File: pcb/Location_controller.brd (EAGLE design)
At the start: 75 x 48 mm, 55 parts, among them IC1 LIS302DL

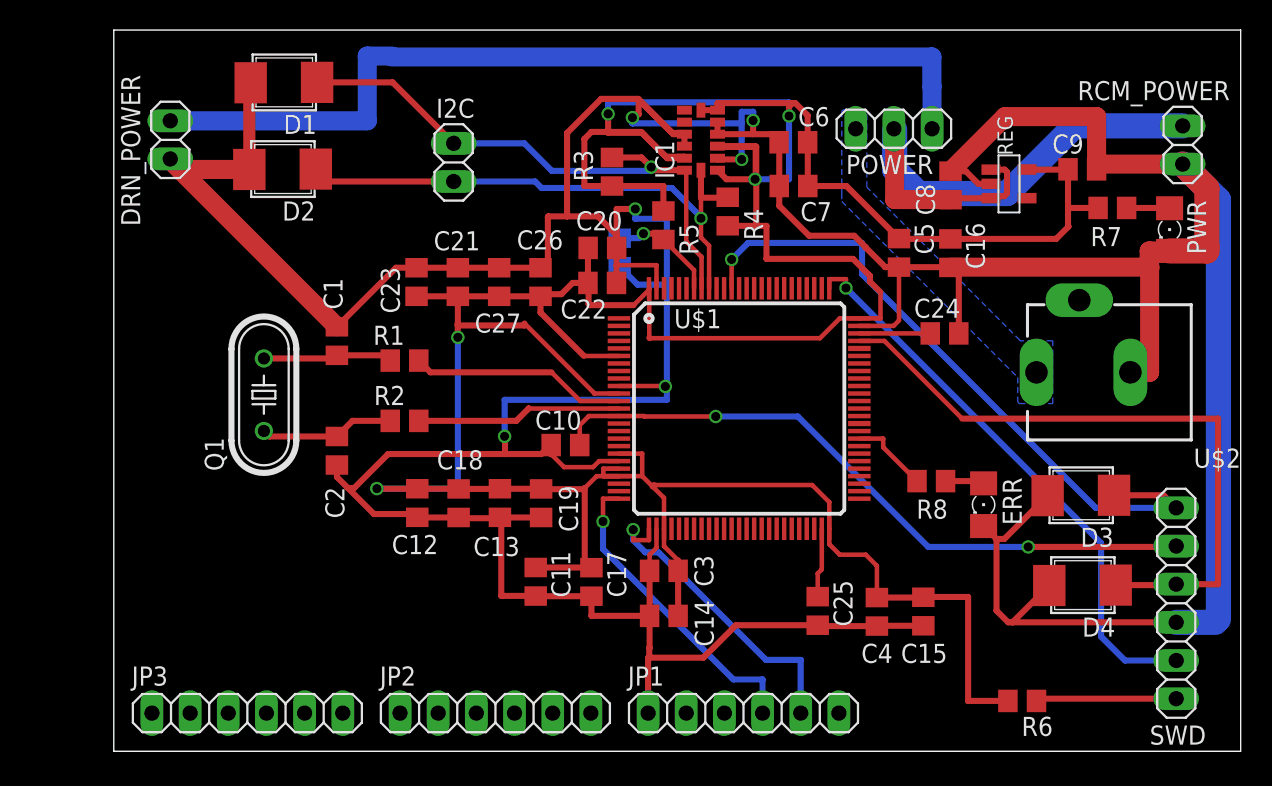
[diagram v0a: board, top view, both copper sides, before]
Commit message: Add TVS for I2C and USART connections
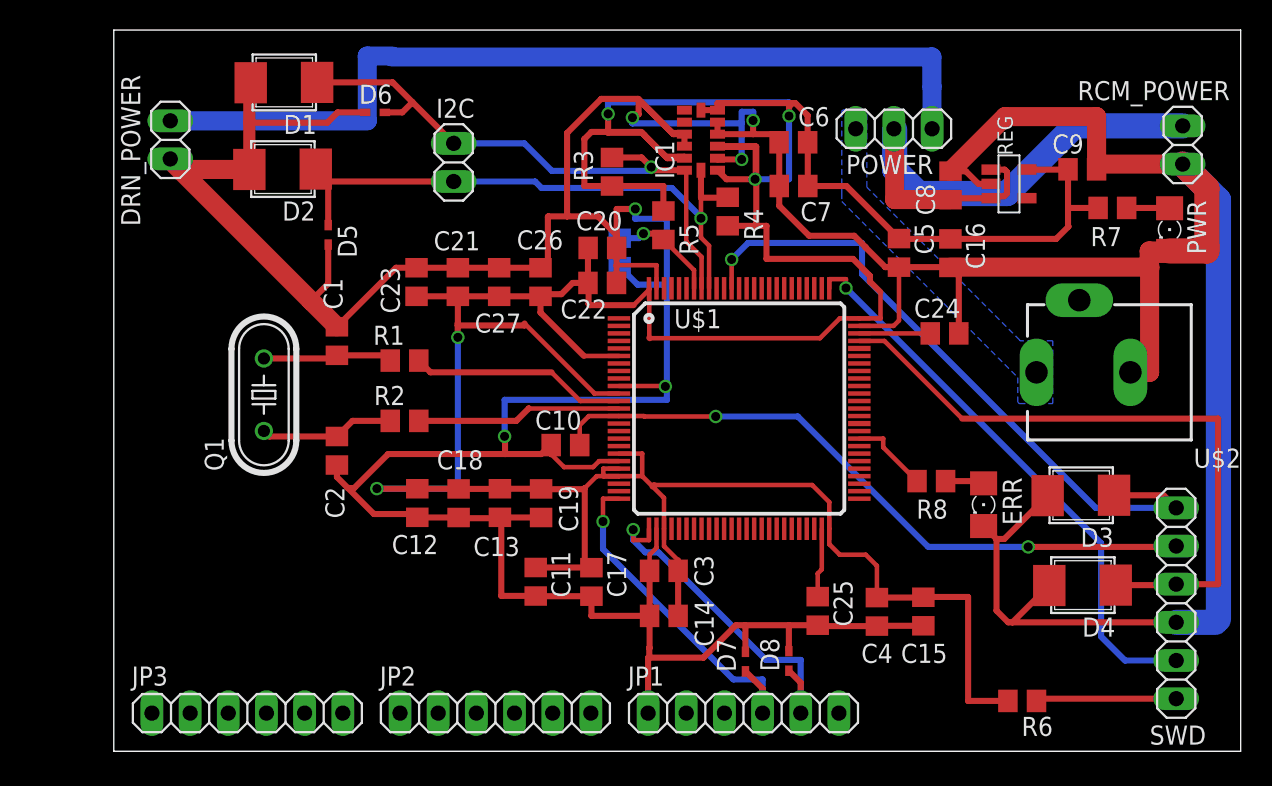
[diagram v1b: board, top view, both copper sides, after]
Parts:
- added D5, D6, D7, D8: (no value), diode:SOD523
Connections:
- net GND: now also D5.A, D6.A, D7.A, D8.A
- net I2C_SCL: now also D5.C
- net I2C_SDA: now also D6.C
- net USART2_RX: now also D8.C
- net USART2_TX: now also D7.C
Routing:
- net GND: track 371.4 -> 387.2 mm
- net USART2_TX: track 20.9 -> 24.1 mm
- net USART2_RX: track 21.2 -> 24.3 mm
- net I2C_SCL: track 36.9 -> 39.8 mm
- net I2C_SDA: track 38.6 -> 40.7 mm
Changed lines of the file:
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@@
 <element name="D4" library="stm32f4" package="SMB" value="ZDIODE" x="64.37" y="10.93" rot="R180"/>
 <element name="D3" library="stm32f4" package="SMB" value="ZDIODE" x="64.26" y="16.91" rot="R180"/>
+<element name="D5" library="diode" package="SOD523" value="" x="14.27" y="34.42" rot="R270"/>
+<element name="D6" library="diode" package="SOD523" value="" x="17.44" y="42.52" smashed="yes" rot="R180">
+<attribute name="NAME" x="18.535" y="44.365" size="1.27" layer="25" rot="R180"/>
+<attribute name="VALUE" x="18.075" y="44.425" size="1.27" layer="27" rot="R180"/>
+</element>
+<element name="D7" library="diode" package="SOD523" value="" x="42.04" y="5.92" rot="R90"/>
+<element name="D8" library="diode" package="SOD523" value="" x="44.93" y="5.96" rot="R90"/>
 </elements>
 <signals>
@@
 <wire x1="36.12" y1="13.54" x2="36.12" y2="14.81" width="0.3048" layer="1"/>
 <wire x1="35.66" y1="9.01" x2="35.66" y2="6.88" width="0.4064" layer="1"/>
-<wire x1="46.85" y1="8.39" x2="41.41" y2="8.39" width="0.4064" layer="1"/>
+<wire x1="46.85" y1="8.39" x2="44.93" y2="8.39" width="0.4064" layer="1"/>
+<wire x1="44.93" y1="8.39" x2="42.02" y2="8.39" width="0.4064" layer="1"/>
+<wire x1="42.02" y1="8.39" x2="41.41" y2="8.39" width="0.4064" layer="1"/>
 <wire x1="49.62" y1="28.31" x2="51.9" y2="28.31" width="0.3048" layer="1"/>
 <wire x1="51.9" y1="28.31" x2="52.26" y2="28.67" width="0.3048" layer="1"/>
@@
 <wire x1="65.21" y1="38.93" x2="65.41" y2="38.73" width="0.4064" layer="1"/>
 <wire x1="3.76" y1="39.42" x2="3.76" y2="39.34" width="0.4064" layer="1"/>
-<wire x1="3.76" y1="39.34" x2="14.85" y2="28.25" width="1.27" layer="1"/>
+<wire x1="3.76" y1="39.34" x2="13.125" y2="29.975" width="1.27" layer="1"/>
+<wire x1="13.125" y1="29.975" x2="14.85" y2="28.25" width="1.27" layer="1"/>
 <wire x1="70.71" y1="8.58" x2="73.32" y2="8.58" width="1.6764" layer="16"/>
 <wire x1="73.32" y1="8.58" x2="73.52" y2="8.78" width="0.4064" layer="16"/>
@@
 <contactref element="D2" pad="2"/>
 <wire x1="9.1118" y1="44.4916" x2="9.0218" y2="44.4916" width="0.4064" layer="1"/>
-<wire x1="9.0218" y1="44.4916" x2="9.0218" y2="38.7216" width="0.8128" layer="1"/>
+<wire x1="9.0218" y1="44.4916" x2="9.0218" y2="41.84" width="0.8128" layer="1"/>
+<wire x1="9.0218" y1="41.84" x2="9.0218" y2="38.7216" width="0.8128" layer="1"/>
 <wire x1="9.0218" y1="38.7216" x2="4.4584" y2="38.7216" width="1.27" layer="1"/>
 <wire x1="4.4584" y1="38.7216" x2="3.76" y2="39.42" width="0.4064" layer="1"/>
@@
 <wire x1="68.91" y1="32.22" x2="68.94" y2="32.22" width="1.27" layer="1"/>
 <wire x1="68.94" y1="32.22" x2="68.94" y2="25.22" width="1.27" layer="1"/>
+<contactref element="D6" pad="A"/>
+<contactref element="D5" pad="A"/>
+<wire x1="16.74" y1="42.52" x2="14.9" y2="42.52" width="0.4064" layer="1"/>
+<wire x1="14.9" y1="42.52" x2="14.22" y2="41.84" width="0.4064" layer="1"/>
+<wire x1="14.22" y1="41.84" x2="9.0218" y2="41.84" width="0.4064" layer="1"/>
+<wire x1="14.27" y1="33.72" x2="14.27" y2="31.12" width="0.4064" layer="1"/>
+<wire x1="14.27" y1="31.12" x2="13.125" y2="29.975" width="0.4064" layer="1"/>
+<contactref element="D7" pad="A"/>
+<contactref element="D8" pad="A"/>
+<wire x1="42.04" y1="6.62" x2="42.04" y2="8.37" width="0.4064" layer="1"/>
+<wire x1="42.04" y1="8.37" x2="42.02" y2="8.39" width="0.4064" layer="1"/>
+<wire x1="44.93" y1="6.66" x2="44.93" y2="8.39" width="0.4064" layer="1"/>
 </signal>
 <signal name="N$1">
@@
 <wire x1="13.4414" y1="38.747" x2="14.2684" y2="37.92" width="0.4064" layer="1"/>
 <wire x1="14.2684" y1="37.92" x2="22.62" y2="37.92" width="0.4064" layer="1"/>
+<contactref element="D5" pad="C"/>
+<wire x1="14.27" y1="35.02" x2="14.27" y2="37.9184" width="0.4064" layer="1"/>
+<wire x1="14.27" y1="37.9184" x2="14.2684" y2="37.92" width="0.4064" layer="1"/>
 </signal>
 <signal name="I2C_SDA">
@@
 <contactref element="D1" pad="1"/>
 <wire x1="13.5314" y1="44.517" x2="18.563" y2="44.517" width="0.4064" layer="1"/>
-<wire x1="18.563" y1="44.517" x2="22.62" y2="40.46" width="0.4064" layer="1"/>
+<wire x1="18.563" y1="44.517" x2="19.88" y2="43.2" width="0.4064" layer="1"/>
+<contactref element="D6" pad="C"/>
+<wire x1="19.88" y1="43.2" x2="22.62" y2="40.46" width="0.4064" layer="1"/>
+<wire x1="18.04" y1="42.52" x2="19.2" y2="42.52" width="0.4064" layer="1"/>
+<wire x1="19.2" y1="42.52" x2="19.88" y2="43.2" width="0.4064" layer="1"/>
 </signal>
 <signal name="N$8">
@@
 <wire x1="41.23" y1="4.78" x2="43.18" y2="4.78" width="0.4064" layer="16"/>
 <wire x1="43.18" y1="4.78" x2="43.18" y2="2.54" width="0.4064" layer="16"/>
+<contactref element="D7" pad="C"/>
+<wire x1="42.04" y1="5.32" x2="43.18" y2="4.18" width="0.4064" layer="1"/>
+<wire x1="43.18" y1="4.18" x2="43.18" y2="2.54" width="0.4064" layer="1"/>
 </signal>
 <signal name="USART2_RX">
@@
 <wire x1="35.62" y1="14.05" x2="34.57" y2="14.05" width="0.3048" layer="1"/>
 <wire x1="34.57" y1="14.05" x2="34.57" y2="14.75" width="0.3048" layer="1"/>
+<contactref element="D8" pad="C"/>
+<wire x1="44.93" y1="5.36" x2="45.72" y2="4.57" width="0.4064" layer="1"/>
+<wire x1="45.72" y1="4.57" x2="45.72" y2="2.54" width="0.4064" layer="1"/>
 </signal>
 <signal name="N$6">

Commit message: Add ground plane
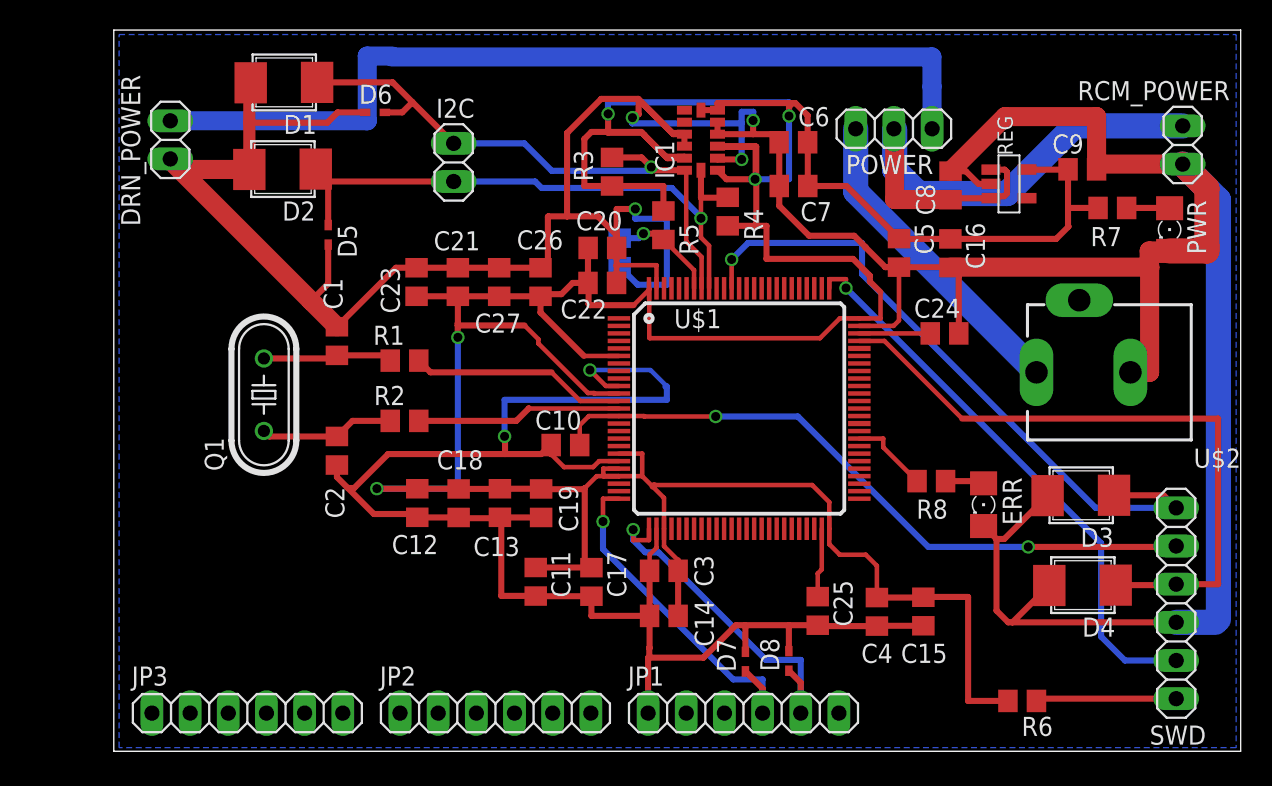
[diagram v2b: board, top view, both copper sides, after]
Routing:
- net N$5: track 0.00 -> 21.2 mm
- net GND: track 387.2 -> 385.2 mm
- added copper zone on layer 16, net GND
- removed copper zone on layer 16, net N$5
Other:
- board text added: "HOP 05 V 1.0"
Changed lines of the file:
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@@
 <wire x1="0" y1="48" x2="0" y2="0" width="0" layer="20"/>
 <text x="47.35" y="43.35" size="1.778" layer="51">BAT</text>
-<text x="52.82" y="43.35" size="1.778" layer="52">DRN</text>
-<text x="15.75" y="39.72" size="1.778" layer="52">SDA</text>
-<text x="15.75" y="37.11" size="1.778" layer="52">SCL</text>
+<text x="52.82" y="43.35" size="1.778" layer="51">DRN</text>
+<text x="15.75" y="39.72" size="1.778" layer="51">SDA</text>
+<text x="15.75" y="37.11" size="1.778" layer="51">SCL</text>
 <circle x="73.38" y="3.44" radius="0.45276875" width="0.4064" layer="51"/>
+<text x="11.14" y="12.44" size="1.778" layer="51" rot="R180">HOP 05
+V 1.0</text>
 </plain>
 <attributes>
@@
 <wire x1="28.44" y1="15.56" x2="25.79" y2="15.56" width="0.4064" layer="1"/>
 <wire x1="25.7" y1="15.56" x2="25.7" y2="15.57" width="0.4064" layer="1"/>
-<wire x1="33.62" y1="24.31" x2="36.71" y2="24.31" width="0.3048" layer="1"/>
-<wire x1="36.71" y1="24.31" x2="36.71" y2="24.28" width="0.4064" layer="1"/>
-<via x="36.71" y="24.28" extent="1-16" drill="0.6" shape="square"/>
 <wire x1="36.71" y1="24.28" x2="36.81" y2="24.28" width="0.4064" layer="16"/>
-<wire x1="36.81" y1="24.28" x2="36.81" y2="31.05" width="0.4064" layer="16"/>
 <wire x1="36.81" y1="31.05" x2="36.81" y2="35.44" width="0.4064" layer="16"/>
 <wire x1="36.81" y1="35.44" x2="34.71" y2="35.44" width="0.4064" layer="16"/>
@@
 <wire x1="42.04" y1="8.37" x2="42.02" y2="8.39" width="0.4064" layer="1"/>
 <wire x1="44.93" y1="6.66" x2="44.93" y2="8.39" width="0.4064" layer="1"/>
+<polygon width="0.4064" layer="16" thermals="no">
+<vertex x="0.35" y="47.7"/>
+<vertex x="74.7" y="47.7"/>
+<vertex x="74.7" y="0.24"/>
+<vertex x="0.35" y="0.24"/>
+</polygon>
+<wire x1="33.62" y1="24.31" x2="32.75" y2="24.31" width="0.3048" layer="1"/>
+<wire x1="32.75" y1="24.31" x2="31.69" y2="25.37" width="0.3048" layer="1"/>
+<via x="31.69" y="25.37" extent="1-16" drill="0.6" shape="square"/>
+<wire x1="31.69" y1="25.37" x2="35.72" y2="25.37" width="0.3048" layer="16"/>
+<wire x1="35.72" y1="25.37" x2="36.81" y2="24.28" width="0.3048" layer="16"/>
 </signal>
 <signal name="N$1">
@@
 <wire x1="33.62" y1="23.81" x2="31.97" y2="23.81" width="0.3048" layer="1"/>
 <wire x1="31.97" y1="23.81" x2="31.97" y2="23.84" width="0.3048" layer="1"/>
-<wire x1="31.97" y1="23.84" x2="27.34" y2="28.47" width="0.3048" layer="1"/>
 <wire x1="22.89" y1="28.47" x2="22.9" y2="28.48" width="0.4064" layer="1"/>
 <wire x1="22.9" y1="28.48" x2="22.9" y2="30.28" width="0.4064" layer="1"/>
@@
 <wire x1="35.62" y1="30.81" x2="35.64" y2="30.79" width="0.3048" layer="1"/>
 <wire x1="35.64" y1="30.79" x2="35.64" y2="27.52" width="0.3048" layer="1"/>
-<wire x1="35.64" y1="27.52" x2="35.67" y2="27.49" width="0.4064" layer="1"/>
+<wire x1="35.64" y1="27.52" x2="35.67" y2="27.49" width="0.3048" layer="1"/>
 <wire x1="35.67" y1="27.49" x2="47" y2="27.49" width="0.3048" layer="1"/>
 <wire x1="47" y1="27.49" x2="48.32" y2="28.81" width="0.3048" layer="1"/>
@@
 <wire x1="17.51" y1="17.48" x2="17.51" y2="17.47" width="0.4064" layer="1"/>
 <wire x1="17.51" y1="17.47" x2="20.2" y2="17.47" width="0.4064" layer="1"/>
-<wire x1="27.34" y1="28.47" x2="27.34" y2="28.34" width="0.4064" layer="1"/>
 <wire x1="27.34" y1="28.34" x2="22.89" y2="28.34" width="0.4064" layer="1"/>
 <wire x1="37.98" y1="39.47" x2="37.98" y2="39.57" width="0.4064" layer="1"/>
@@
 <contactref element="R5" pad="1"/>
 <wire x1="36.58" y1="35.96" x2="36.58" y2="37.62" width="0.4064" layer="1"/>
+<wire x1="31.97" y1="23.84" x2="31.56" y2="23.84" width="0.3048" layer="1"/>
+<wire x1="31.56" y1="23.84" x2="28.26" y2="27.14" width="0.3048" layer="1"/>
+<wire x1="28.26" y1="27.14" x2="28.26" y2="27.42" width="0.3048" layer="1"/>
+<wire x1="28.26" y1="27.42" x2="27.34" y2="28.34" width="0.3048" layer="1"/>
 </signal>
 <signal name="I2C_SCL">
@@
 <contactref element="POWER" pad="1"/>
 <contactref element="U$2" pad="PWR"/>
-<polygon width="0.4064" layer="16" thermals="no">
-<vertex x="60.92" y="23.14"/>
-<vertex x="62.49" y="23.14"/>
-<vertex x="62.49" y="27.32"/>
-<vertex x="60.3" y="27.32"/>
-<vertex x="60.3" y="27.36"/>
-<vertex x="50.12" y="37.54"/>
-<vertex x="50.12" y="42.62"/>
-<vertex x="50.05" y="42.69"/>
-<vertex x="48.55" y="42.69"/>
-<vertex x="48.45" y="42.59"/>
-<vertex x="48.45" y="37.15"/>
-<vertex x="48.45" y="36.59"/>
-<vertex x="60.16" y="24.88"/>
-<vertex x="60.16" y="23.25"/>
-<vertex x="60.27" y="23.14"/>
-</polygon>
+<wire x1="49.38" y1="41.43" x2="49.38" y2="37.25" width="1.6764" layer="16"/>
+<wire x1="49.38" y1="37.25" x2="61.41" y2="25.22" width="1.6764" layer="16"/>
 </signal>
 <signal name="IN_3V">
@@
 </board>
 </drawing>
+<compatibility>
+<note version="6.3" minversion="6.2.2" severity="warning">
+Since Version 6.2.2 text objects can contain more than one line,
+which will not be processed correctly with this version.
+</note>
+</compatibility>
 </eagle>

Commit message: Add ground plane on top
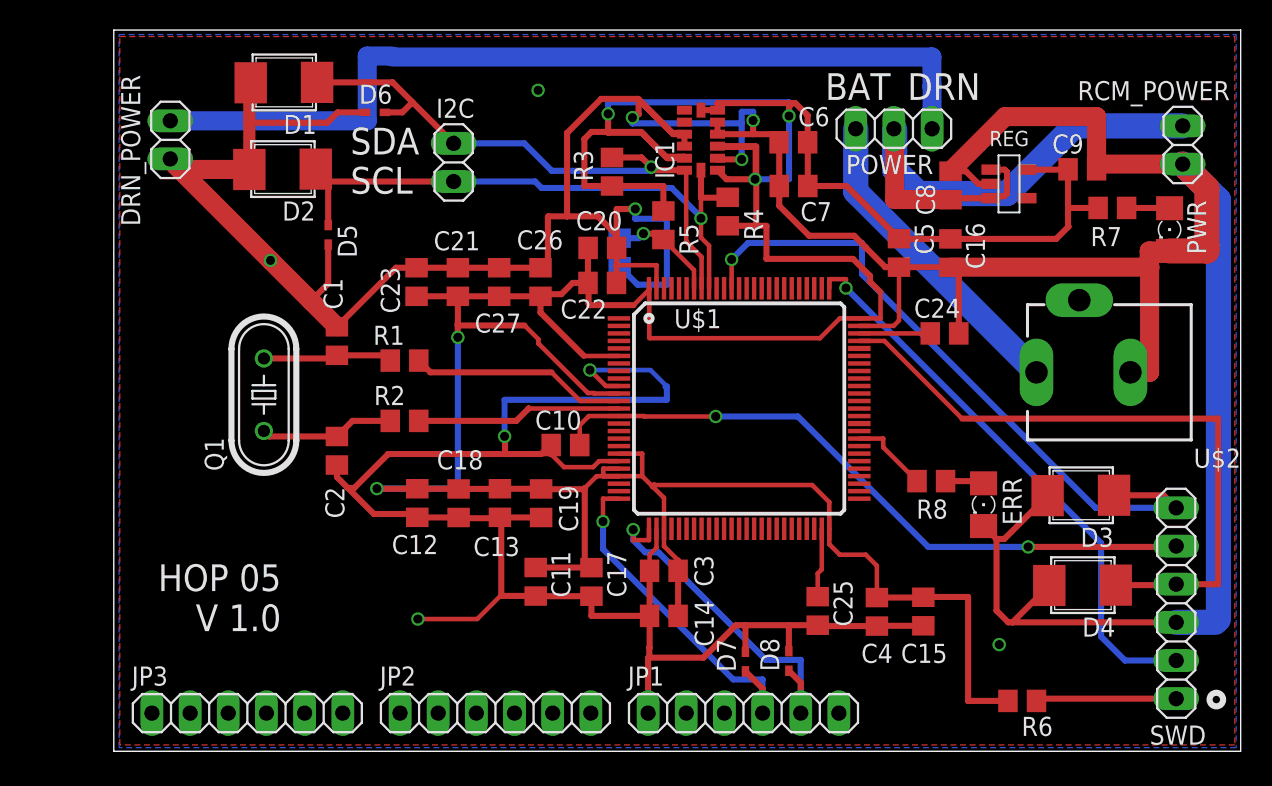
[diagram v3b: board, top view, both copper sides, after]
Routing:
- net GND: track 385.2 -> 391.5 mm, vias 6 -> 10
- added copper zone on layer 1, net GND
